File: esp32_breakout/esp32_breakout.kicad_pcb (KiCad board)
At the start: 2 copper layers, 73.1 x 33.1 mm, 25 parts, among them J1 JST B5B-PH-K-S, J10 JST B6B-PH-K-S, J2 JST B5B-PH-K-S, J3 JST B7B-PH-K-S, J4 XT30U-M, J5 HDR M VERT 12p 2.54mm, J9 JST B6B-PH-K-S, SW1 SS12D10, U1 ESP32 DEV KIT Module 30-pin, U2 LM2596 Module

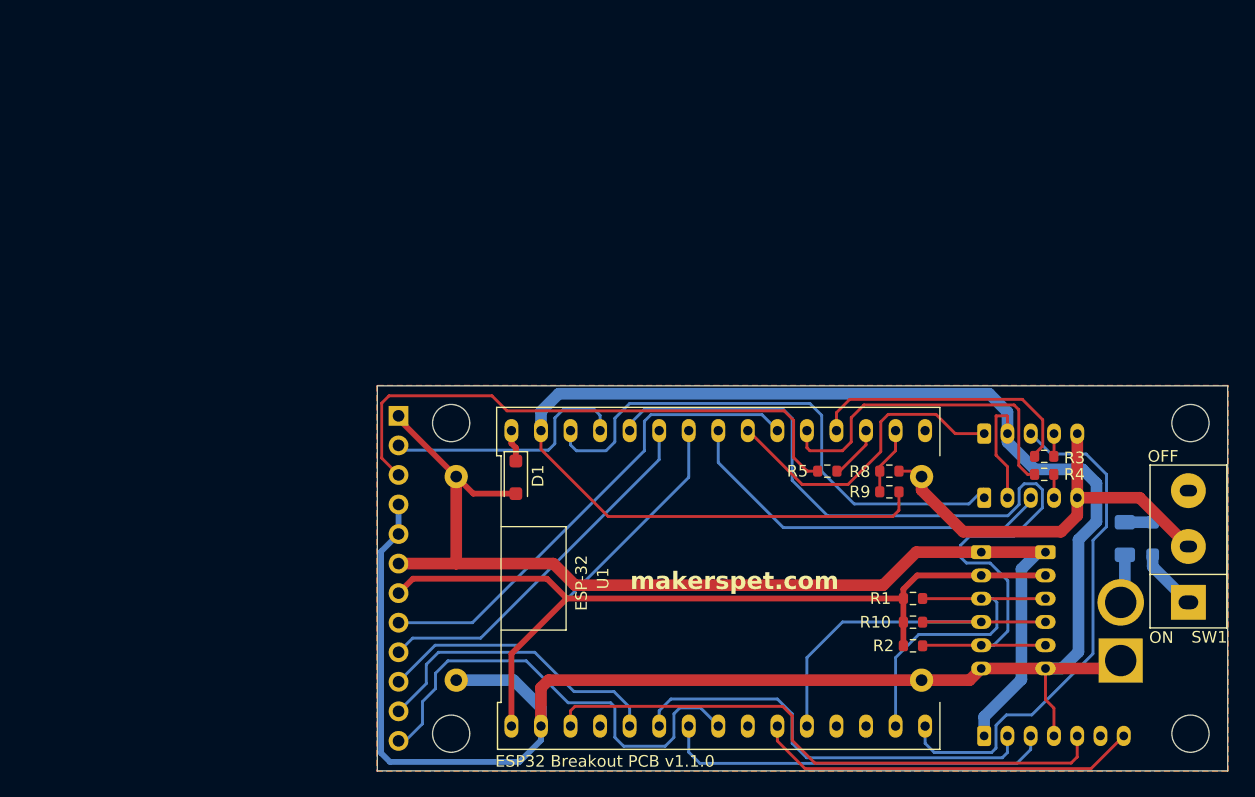
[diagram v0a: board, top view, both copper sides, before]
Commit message: ZH extension connector; 6-pin LDS connector
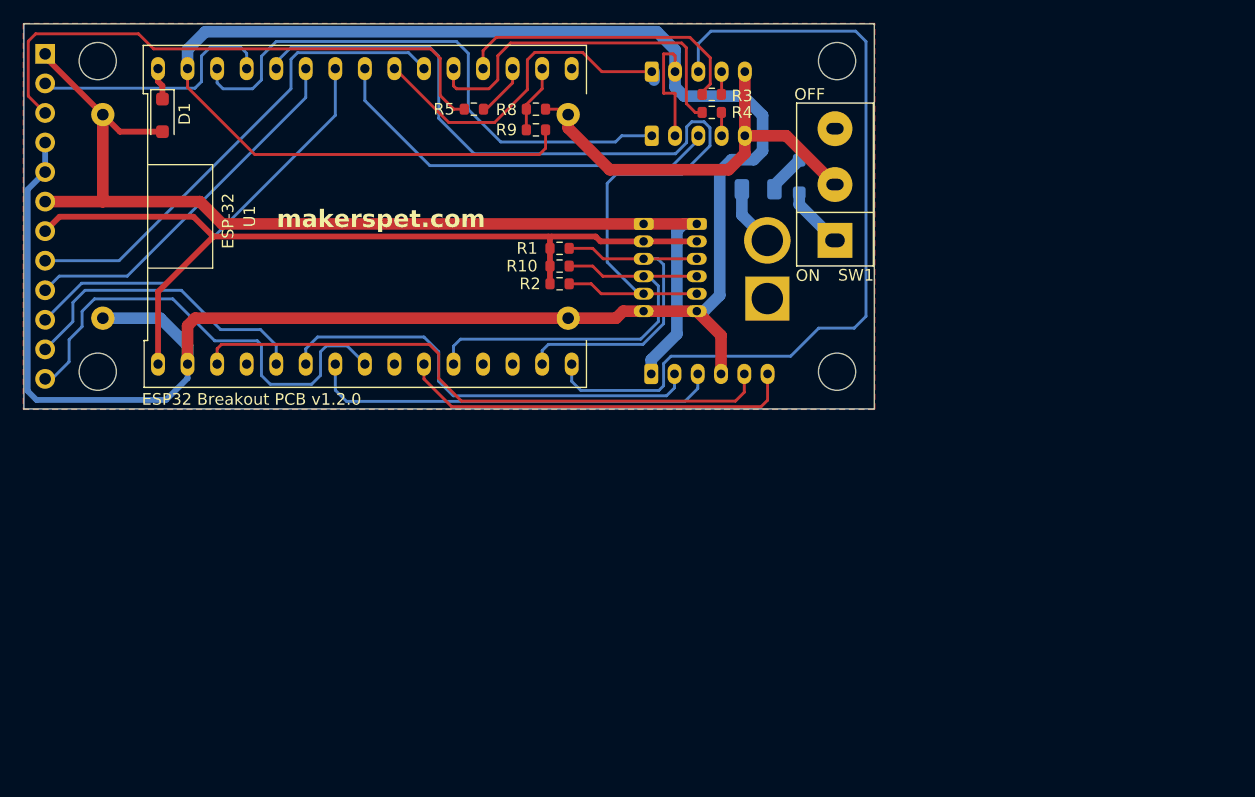
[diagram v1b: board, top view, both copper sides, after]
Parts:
- J10, J9: value JST B6B-PH-K-S -> JST B6B-ZR; footprint Connector_JST:JST_PH_B6B-PH-K_1x06_P2.00mm_Vertical -> Makerspet:JST_ZH_B6B-ZR_1x06_P1.50mm_Vertical
- J3: value JST B7B-PH-K-S -> JST B6B-PH-K-S; footprint Connector_JST:JST_PH_B7B-PH-K_1x07_P2.00mm_Vertical -> Connector_JST:JST_PH_B6B-PH-K_1x06_P2.00mm_Vertical
- moved F1 43.5 mm to (155.1, 62.9), turned to 0 degrees
- moved R9 43.5 mm to (136.0, 57.8)
- moved R8 43.5 mm to (136.0, 56.0)
- moved D2 43.5 mm to (158.6, 61.8)
- moved H1 43.5 mm to (98.3, 51.8)
- moved H2 43.5 mm to (161.8, 51.8)
- moved J5 43.5 mm to (93.8, 51.2)
- moved R2 43.5 mm to (138.0, 71.0)
- moved SW1 43.5 mm to (161.7, 62.5)
- moved D1 43.5 mm to (103.9, 56.5)
- moved H3 43.5 mm to (161.8, 78.5)
- moved H4 43.5 mm to (98.3, 78.5)
- moved J4 43.5 mm to (155.9, 72.3)
- moved R5 43.5 mm to (130.6, 56.0)
- moved U1 43.5 mm to (121.3, 65.2)
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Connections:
- J3 pad 6: unconnected-(J3-Pin_6-Pad6) -> /LDS_EN
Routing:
- net /MOT_CW_LEFT: track 44.8 -> 72.1 mm
- net +5V: track 97.0 -> 93.1 mm
- net /I2C_SDA: track 32.7 -> 36.0 mm
- net /I2C_INT: track 79.1 -> 81.4 mm
- net /MOT_PWM_LEFT: track 26.9 -> 29.2 mm
- net /MOT_FG_RIGHT: track 29.3 -> 31.2 mm
- net /LDS_RX: track 33.7 -> 35.6 mm
- net /MOT_FG_LEFT: track 23.9 -> 25.5 mm
- net /LDS_TX: track 36.8 -> 38.4 mm
- net /LDS_MOT_PWM: track 50.3 -> 51.9 mm
- net /MOT_PWM_RIGHT: track 46.8 -> 48.3 mm
- net GND: track 228.5 -> 227.4 mm
- net /LDS_EN: track 33.2 -> 34.3 mm
- net Net-(J4-+): track 4.24 -> 5.30 mm
- net /I2C_SCL: track 29.8 -> 30.9 mm
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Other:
- board text added: "ESP32 Breakout PCB v1.2.0"
- board text removed: "ESP32 Breakout PCB v1.1.0"

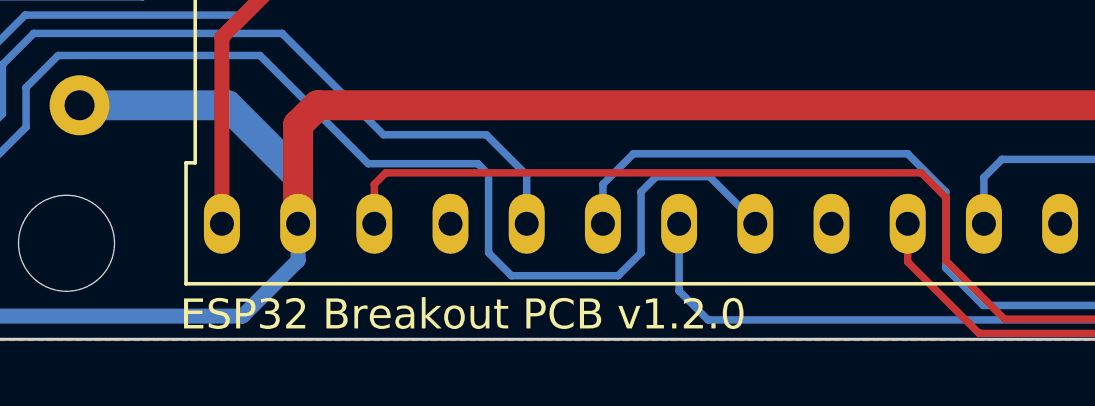
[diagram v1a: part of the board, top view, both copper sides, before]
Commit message: 12V motors
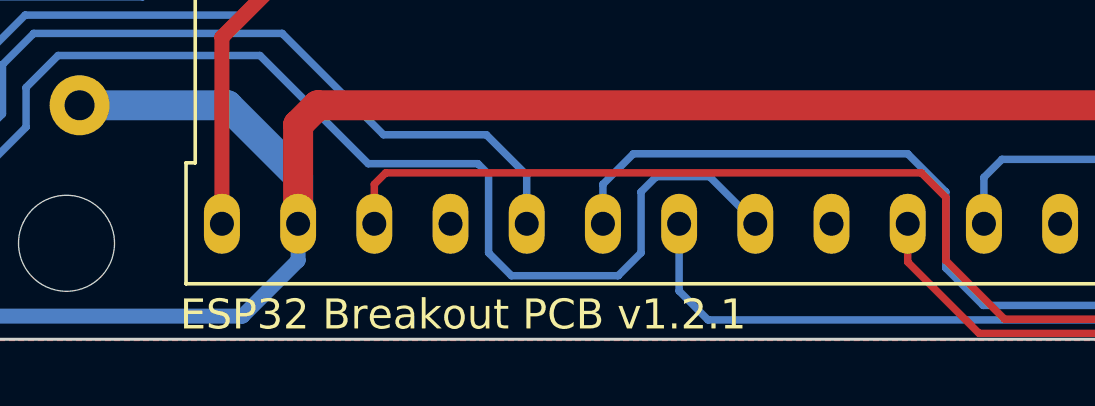
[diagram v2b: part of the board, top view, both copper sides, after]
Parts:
- R9: value 10k -> 20k
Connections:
- net +24V renamed Vdrive
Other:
- board text added: "ESP32 Breakout PCB v1.2.1"
- board text removed: "ESP32 Breakout PCB v1.2.0"
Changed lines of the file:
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@@
   (title_block
     (title "ESP32 Breakout Board")
-    (date "2024-03-06")
-    (rev "1.2.0")
+    (date "2024-03-11")
+    (rev "1.2.1")
     (company "makerspet.com")
   )
@@
   (net 4 "/MOT_CW_RIGHT")
   (net 5 "Net-(J1-Pin_4)")
-  (net 6 "+24V")
+  (net 6 "Vdrive")
   (net 7 "/MOT_PWM_LEFT")
   (net 8 "/MOT_CW_LEFT")
@@
       (net 20 "Net-(D2-K)") (pinfunction "A") (pintype "passive"))
     (pad "2" thru_hole circle (at 0 0 90) (size 3 3) (drill oval 1 1.5) (layers "*.Cu" "*.Mask")
-      (net 6 "+24V") (pinfunction "B") (pintype "passive"))
+      (net 6 "Vdrive") (pinfunction "B") (pintype "passive"))
     (pad "3" thru_hole circle (at 4.8 0 90) (size 3 3) (drill oval 1 1.5) (layers "*.Cu" "*.Mask")
       (net 29 "unconnected-(SW1-C-Pad3)") (pinfunction "C") (pintype "passive+no_connect"))
@@
       (net 28 "/BAT_ADC") (pintype "passive"))
     (pad "2" smd roundrect (at 0.825 0) (size 0.8 0.95) (layers "F.Cu" "F.Paste" "F.Mask") (roundrect_rratio 0.25)
-      (net 6 "+24V") (pintype "passive"))
+      (net 6 "Vdrive") (pintype "passive"))
     (model "${KICAD6_3DMODEL_DIR}/Resistor_SMD.3dshapes/R_0603_1608Metric.wrl"
       (offset (xyz 0 0 0))
@@
         (effects (font (size 1 1) (thickness 0.15)))
     )
-    (fp_text value "10k" (at 0 1.43 -360) (layer "F.Fab") hide
+    (fp_text value "20k" (at 0 1.43 -360) (layer "F.Fab") hide
         (effects (font (size 1 1) (thickness 0.15)))
     )
@@
       (net 5 "Net-(J1-Pin_4)") (pinfunction "Pin_4") (pintype "passive"))
     (pad "5" thru_hole oval (at 8 0) (size 1.2 1.75) (drill 0.75) (layers "*.Cu" "*.Mask")
-      (net 6 "+24V") (pinfunction "Pin_5") (pintype "passive"))
+      (net 6 "Vdrive") (pinfunction "Pin_5") (pintype "passive"))
     (model "${KICAD6_3DMODEL_DIR}/Connector_JST.3dshapes/JST_PH_B5B-PH-K_1x05_P2.00mm_Vertical.wrl"
       (offset (xyz 0 0 0))
@@
       (net 1 "+5V") (pinfunction "VOUT+") (pintype "power_out"))
     (pad "4" thru_hole circle (at -20 8.75 180) (size 2 2) (drill 1) (layers "*.Cu" "*.Mask")
-      (net 6 "+24V") (pinfunction "VIN+") (pintype "power_in"))
+      (net 6 "Vdrive") (pinfunction "VIN+") (pintype "power_in"))
     (model "C:/Users/ilya/git/pcb/step/LM2596 DC-DC StepDown Converter v1.step"
       (offset (xyz 21.5 -0.5 12.5))
@@
       (net 9 "Net-(J2-Pin_4)") (pinfunction "Pin_4") (pintype "passive"))
     (pad "5" thru_hole oval (at 8 0) (size 1.2 1.75) (drill 0.75) (layers "*.Cu" "*.Mask")
-      (net 6 "+24V") (pinfunction "Pin_5") (pintype "passive"))
+      (net 6 "Vdrive") (pinfunction "Pin_5") (pintype "passive"))
     (model "${KICAD6_3DMODEL_DIR}/Connector_JST.3dshapes/JST_PH_B5B-PH-K_1x05_P2.00mm_Vertical.wrl"
       (offset (xyz 0 0 0))
@@
     (effects (font (size 1.5 1.5) (thickness 0.3) bold) (justify bottom))
   )
-  (gr_text "ESP32 Breakout PCB v1.2.0" (at 102.0826 81.5086) (layer "F.SilkS")
+  (gr_text "ESP32 Breakout PCB v1.2.1" (at 102.0826 81.5086) (layer "F.SilkS")
     (effects (font (size 1 1) (thickness 0.15)) (justify left bottom))
   )

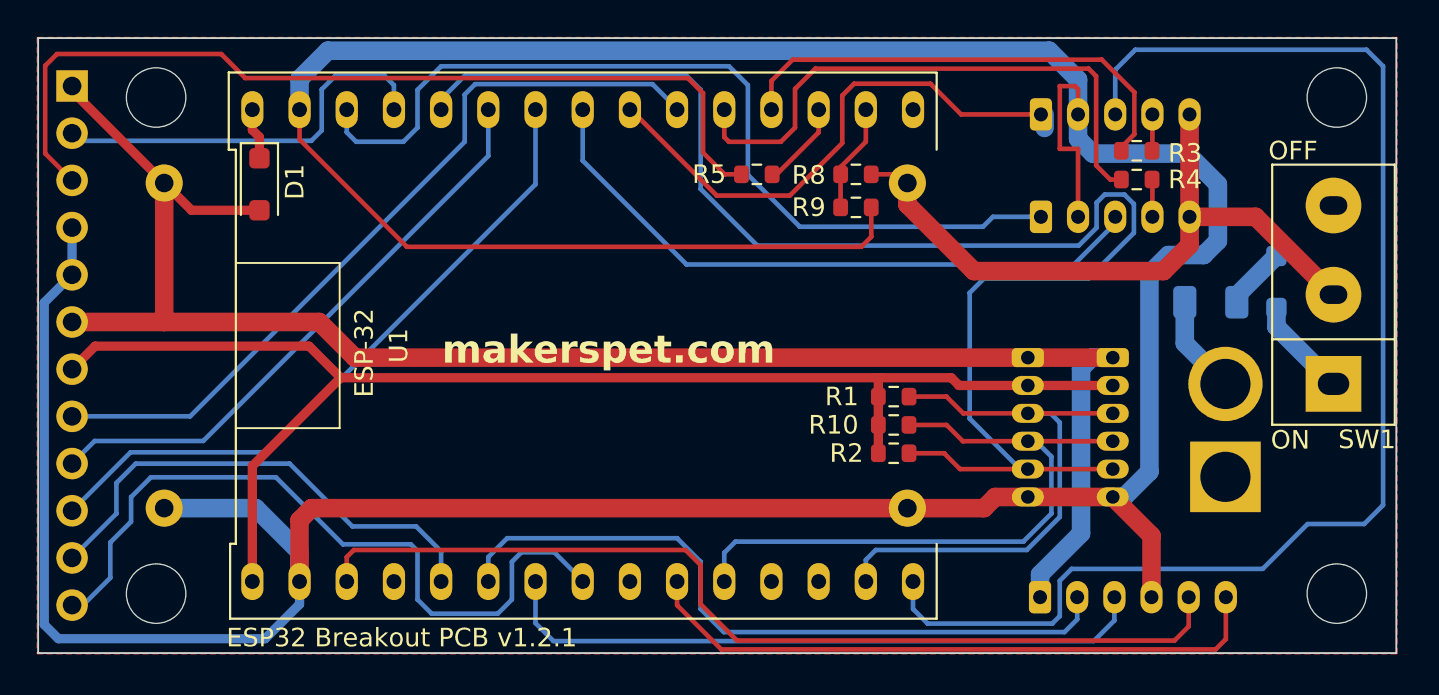
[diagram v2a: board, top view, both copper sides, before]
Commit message: Brushed, quad-encoder motors
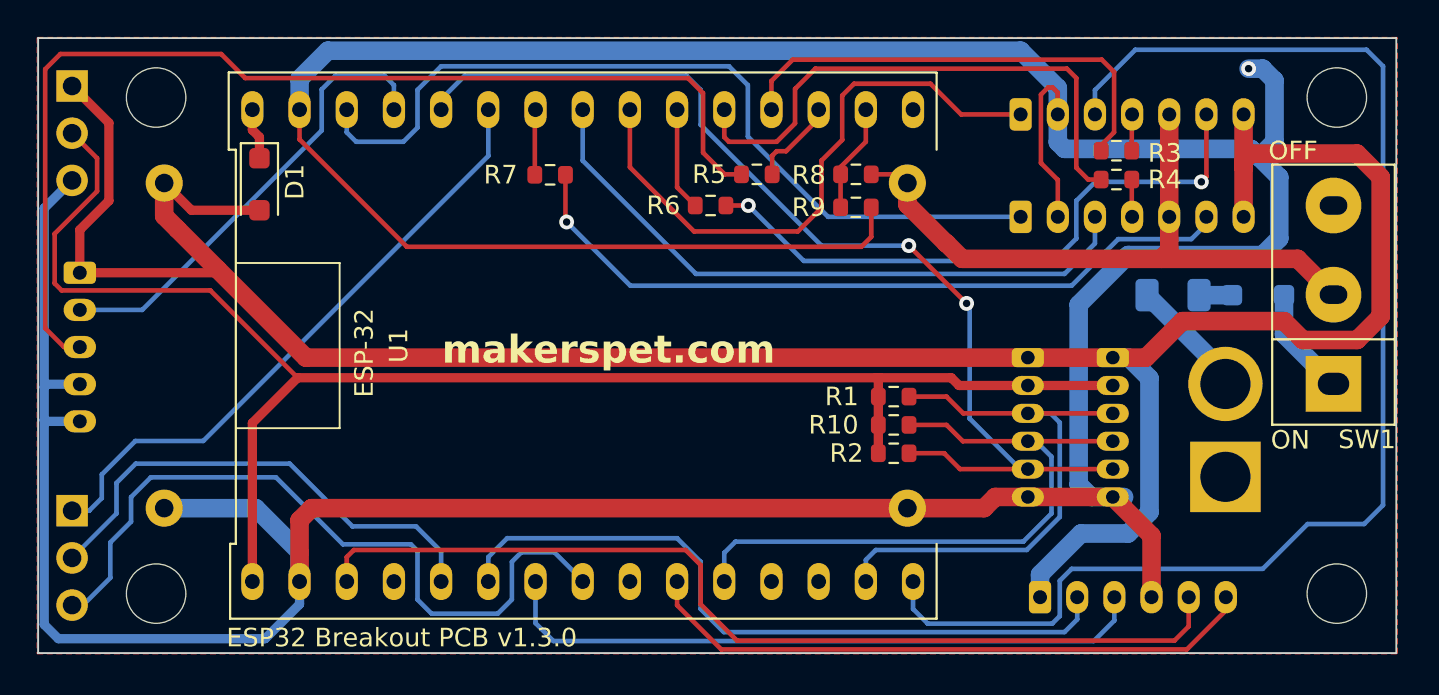
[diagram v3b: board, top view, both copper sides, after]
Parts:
- added J6: DNP, Connector_PinSocket_2.54mm:PinSocket_1x03_P2.54mm_Vertical, B.Cu at (93.8, 74.1)
- added J7: DNP, Connector_PinSocket_2.54mm:PinSocket_1x03_P2.54mm_Vertical, B.Cu at (93.8, 51.2)
- added R6: 10k, Resistor_SMD:R_0603_1608Metric, F.Cu at (128.1, 57.7)
- added R7: 10k, Resistor_SMD:R_0603_1608Metric, F.Cu at (119.5, 56.0)
- J1, J2: value JST B5B-PH-K-S -> JST B7B-PH-K-S; footprint Connector_JST:JST_PH_B5B-PH-K_1x05_P2.00mm_Vertical -> Connector_JST:JST_PH_B7B-PH-K_1x07_P2.00mm_Vertical
- J5: value HDR M VERT 12p 2.54mm -> JST B5B-PH-K-S; footprint Connector_PinSocket_2.54mm:PinSocket_1x12_P2.54mm_Vertical -> Connector_JST:JST_PH_B5B-PH-K_1x05_P2.00mm_Vertical
- moved J5 10.1 mm to (94.2, 61.3), turned to -90 degrees
- moved F1 2.07 mm to (153.0, 62.5)
- moved D2 1.22 mm to (157.6, 62.5), turned to 180 degrees
- moved J1 1.09 mm to (144.8, 58.3)
- moved J2 1.09 mm to (144.8, 52.8)
- moved R3 1.09 mm to (150.0, 54.7)
- moved R4 1.09 mm to (150.0, 56.3)
- renumbered J9 to J8, J10 to J9
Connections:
- net /MOT_CW_LEFT renamed /MOT_CW_LEFT_IN2
- net /MOT_CW_RIGHT renamed /MOT_CW_RIGHT_IN4
- net /MOT_FG_LEFT renamed /MOT_FG_LEFT_ENC_A
- net /MOT_FG_RIGHT renamed /MOT_FG_RIGHT_ENC_A
- net /MOT_PWM_LEFT renamed /MOT_PWM_LEFT_IN1
- net /MOT_PWM_RIGHT renamed /MOT_PWM_RIGHT_IN3
- U1 pad 21: /GPIO32_TOUCH -> /ENC_B_LEFT
- U1 pad 24: /GPIO26_TOUCH -> /ENC_B_RIGHT
- U1 pad 25: /GPIO27_TOUCH -> /GPIO27
- U1 pad 5: /GPIO4_TOUCH -> /GPIO4
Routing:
- net +5V: track 93.1 -> 136.5 mm
- net /GPIO32_TOUCH: track 42.0 -> 0.00 mm
- net Net-(J1-Pin_6): track 0.00 -> 40.2 mm, vias 0 -> 1
- net /GPIO26_TOUCH: track 36.3 -> 0.00 mm
- net /GPIO27: track 0.00 -> 33.6 mm
- net Net-(J2-Pin_6): track 0.00 -> 33.5 mm, vias 0 -> 2
- net /GPIO27_TOUCH: track 31.8 -> 0.00 mm
- net /GPIO4_TOUCH: track 26.5 -> 0.00 mm
- net /GPIO4: track 0.00 -> 26.5 mm
- net /I2C_INT: track 81.4 -> 57.3 mm, vias 0 -> 2
- net GND: track 227.4 -> 248.0 mm, vias 0 -> 1
- net +3V3: track 74.8 -> 85.3 mm
- net Net-(J5-Pin_3): track 49.1 -> 58.6 mm
- net /ENC_B_LEFT: track 0.00 -> 5.62 mm
- net /ENC_B_RIGHT: track 0.00 -> 3.52 mm
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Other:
- board text added: "ESP32 Breakout PCB v1.3.0"
- board text added: "EXPANSION"
- board text added: "L MOTOR R"
- board text removed: "ESP32 Breakout PCB v1.2.1"
- board text removed: "EXT"
- board text removed: "LEFT RIGHT"
- board text removed: "MOTORS"

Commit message: Cleanup
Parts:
- moved F1 13.0 mm to (161.2, 72.6)
- moved D2 8.52 mm to (161.2, 70.2), turned to 0 degrees
- moved J4 4.96 mm to (155.7, 67.3), turned to -90 degrees
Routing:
- net GND: track 248.0 -> 173.6 mm, vias 1 -> 6
- net Net-(J4-+): track 6.53 -> 4.20 mm
- net Net-(D2-K): track 5.88 -> 3.76 mm
- net /LDS_MOT_PWM: track 51.9 -> 50.5 mm
- net /LDS_EN: track 33.4 -> 32.7 mm
- net Net-(D2-A): track 1.77 -> 2.41 mm
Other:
- board text added: "+BATT"
- board text removed: "+BATT-"
